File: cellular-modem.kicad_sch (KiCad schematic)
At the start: 44 parts, among them J1 Conn_Coaxial, J2 SIM8060-6-1-14-00-A, Q1 BC818, SW1 KMR221GLFS, U2 EG25G

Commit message: Add: Improved layout
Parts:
- removed J1: Conn_Coaxial, Connector_Coaxial:U.FL_Hirose_U.FL-R-SMT-1_Vertical, symbol Connector:Conn_Coaxial
- removed TP3: DCD, TestPoint:TestPoint_Pad_D1.5mm, symbol Connector:TestPoint
- removed TP4: CTS, TestPoint:TestPoint_Pad_D1.5mm, symbol Connector:TestPoint
- removed TP5: RTS, TestPoint:TestPoint_Pad_D1.5mm, symbol Connector:TestPoint
- removed TP6: DTR, TestPoint:TestPoint_Pad_D1.5mm, symbol Connector:TestPoint
- added E1: NN02-201, NN02-201:XCVR_NN02-201, symbol NN02-201:NN02-201
- TP1, TP10, TP7, TP8, TP9: footprint TestPoint:TestPoint_Pad_D1.5mm -> TestPoint:TestPoint_Pad_1.0x1.0mm
- TP2: value RI -> 3V8; footprint TestPoint:TestPoint_Pad_D1.5mm -> TestPoint:TestPoint_Pad_1.0x1.0mm
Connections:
- net +3V8: now also TP2.1
- net at C14.1, L2.1: now also E1.1
- net at U2.62 (RI): no longer TP2.1
- no-connect marks 54 -> 59

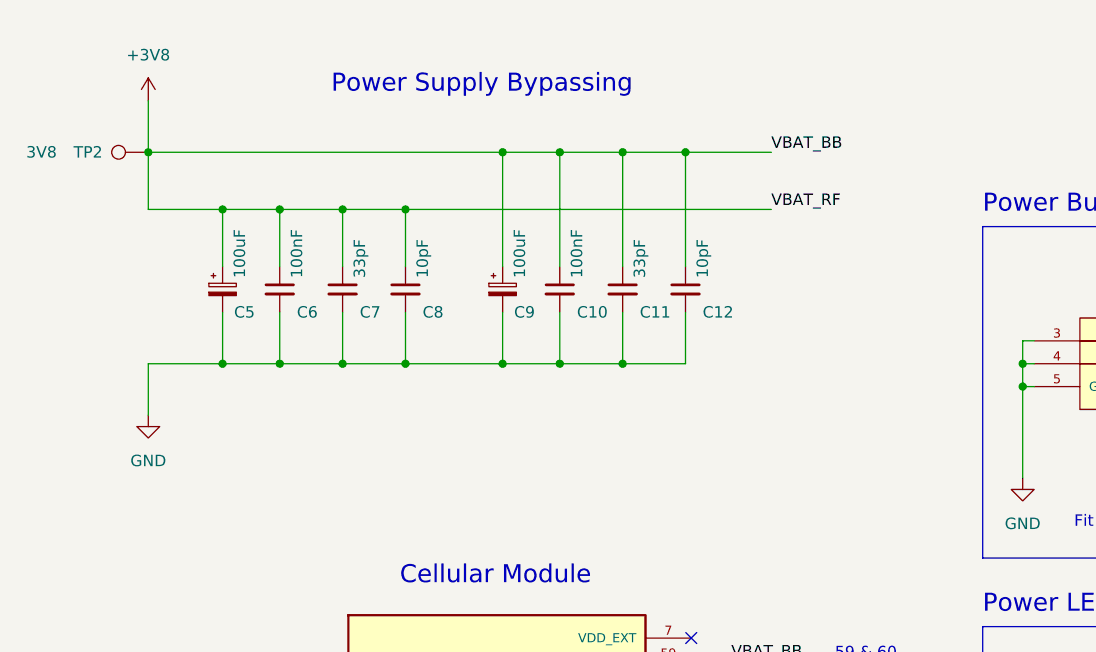
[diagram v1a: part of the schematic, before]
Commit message: Update: Ground plane setup
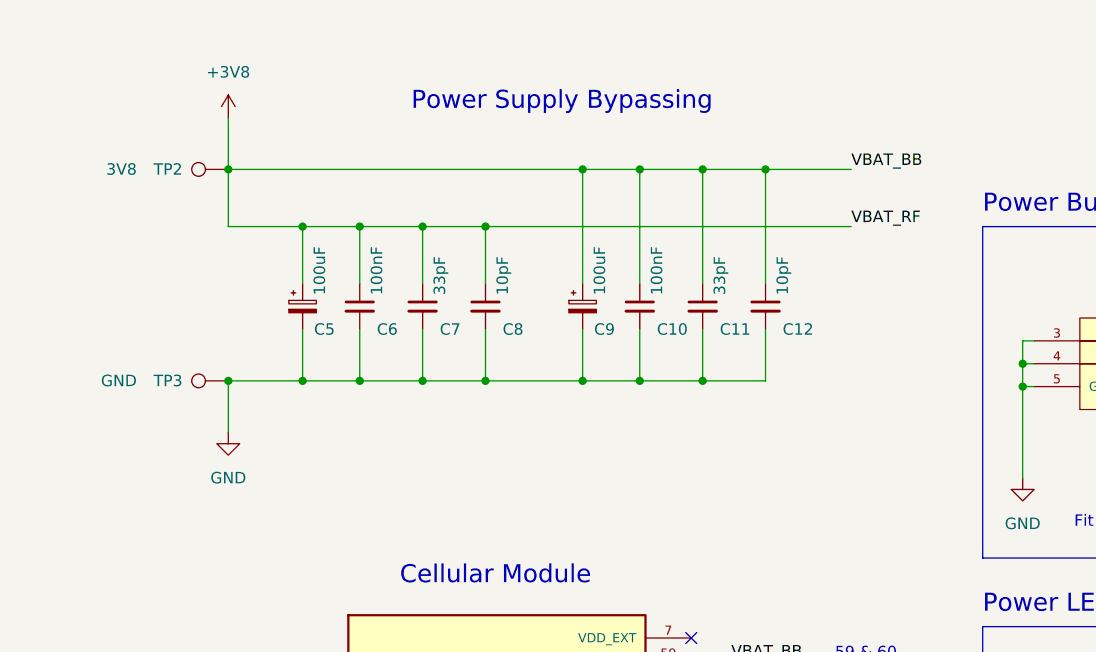
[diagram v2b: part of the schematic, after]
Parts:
- added TP3: GND, TestPoint:TestPoint_Pad_1.0x1.0mm, symbol Connector:TestPoint
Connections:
- net GND: now also TP3.1
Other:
- moved on the sheet: C10, C11, C12, C5, C6, C7, C8, C9, TP2

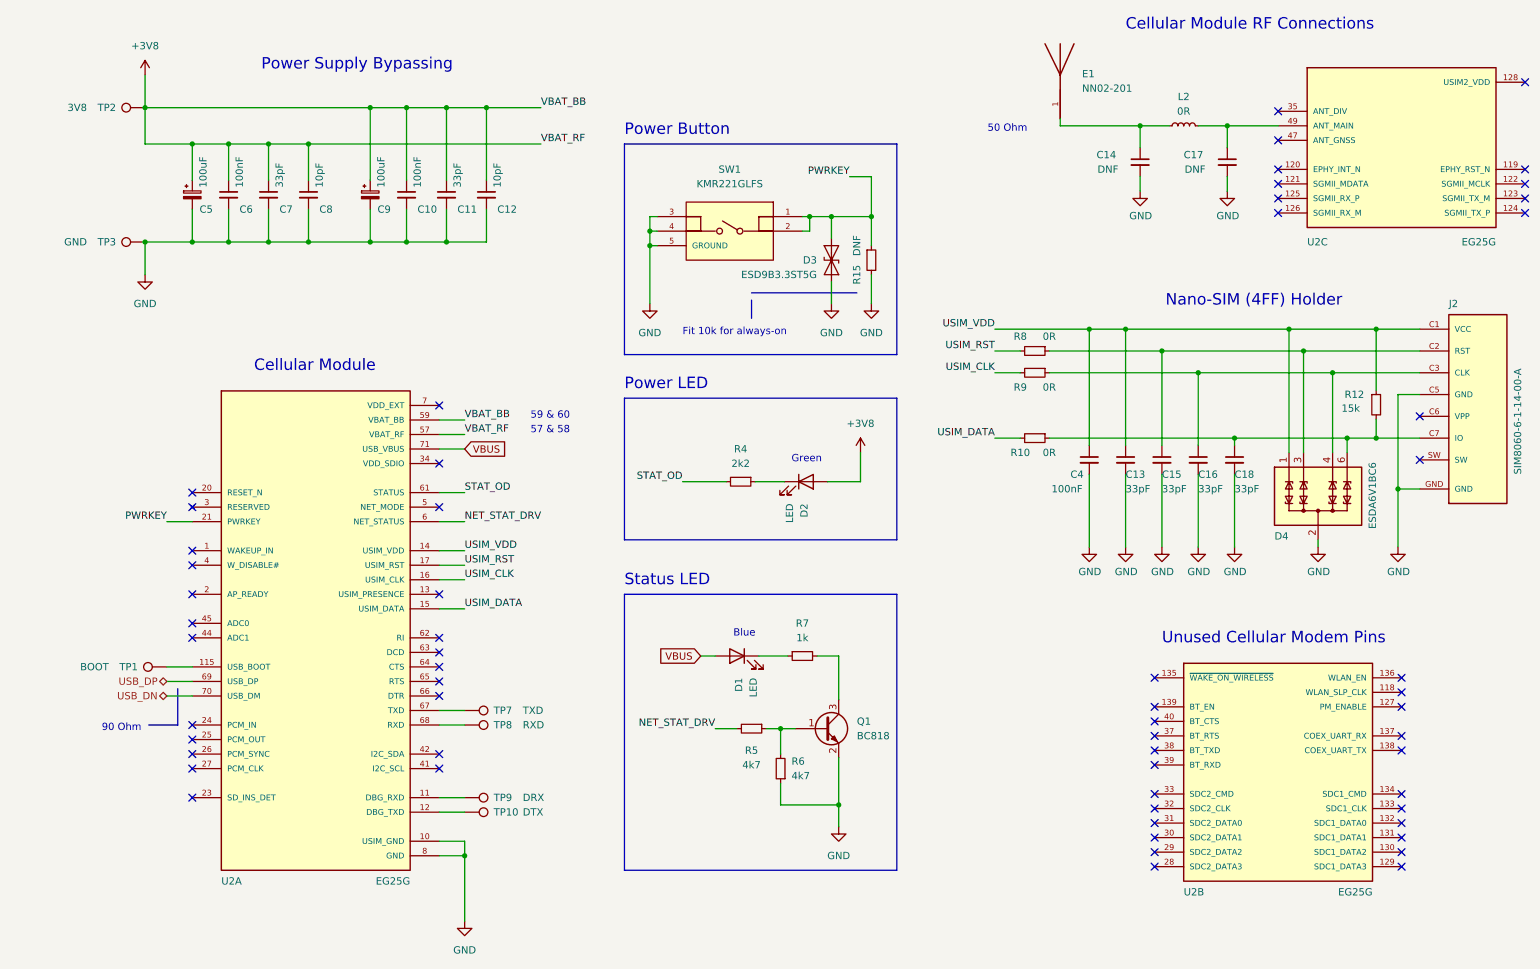
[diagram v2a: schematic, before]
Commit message: Add: Board size changes
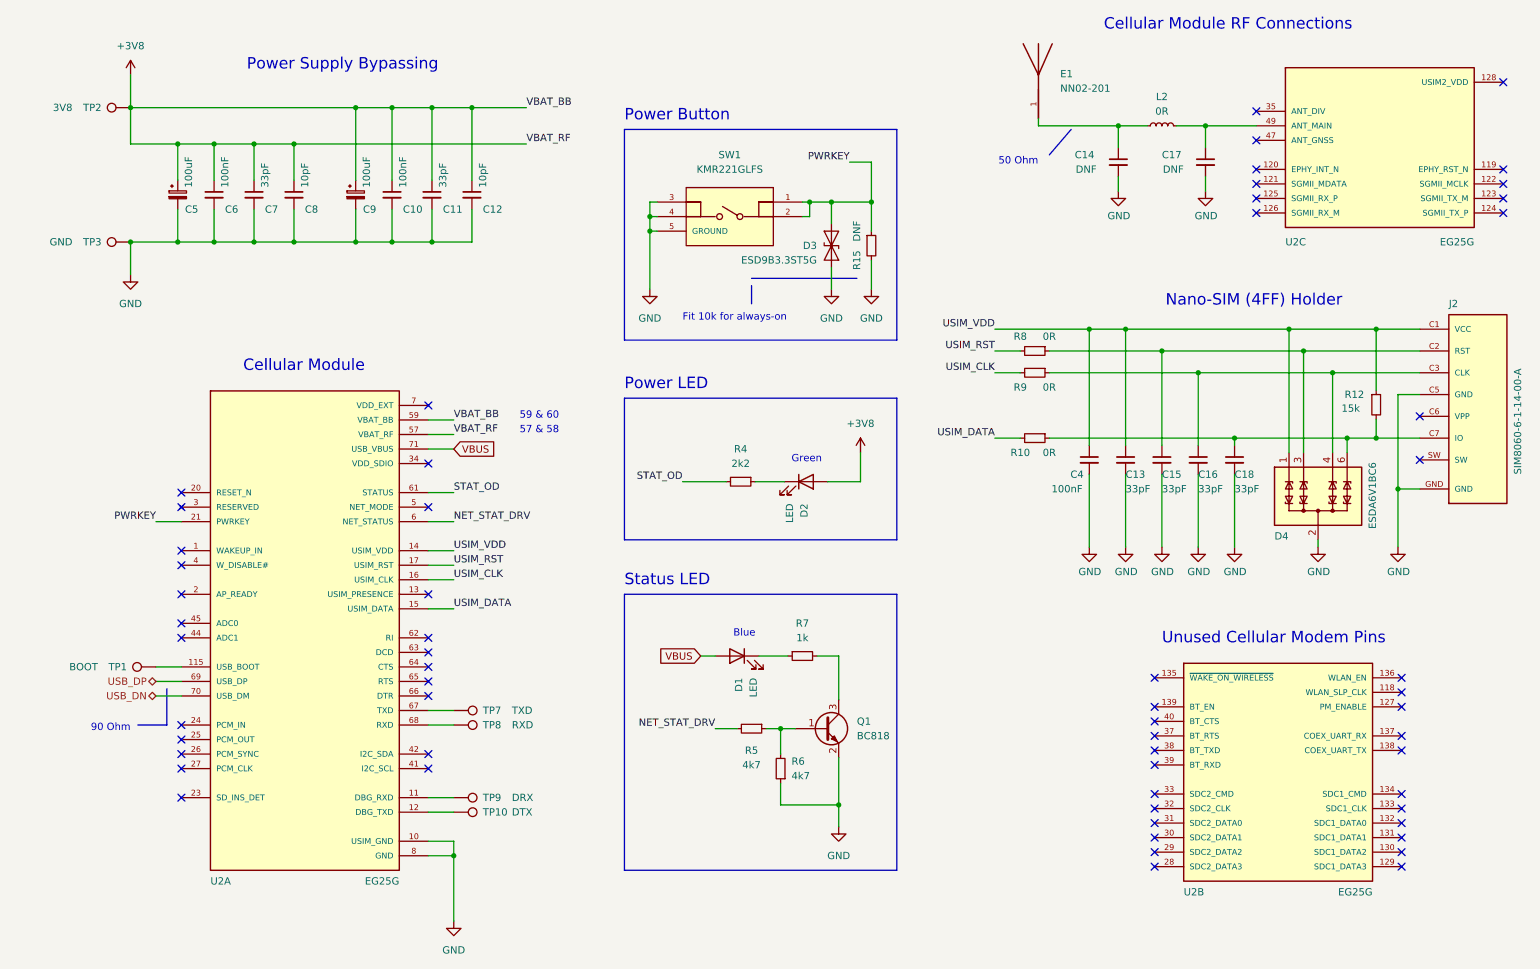
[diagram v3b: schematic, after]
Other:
- moved on the sheet: C10, C11, C12, C14, C17, C5, C6, C7, C8, C9, D3, E1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

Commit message: Change: Separate boards rather than using mousebites
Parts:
- C10, C4, C6: Int @ 10 (none) -> 0.038; MPN (none) -> C0603C104K3RAC; Mfr (none) -> KEMET; SKU (none) -> 80-C0603C104K3RAC; Stock Situation (none) -> OK @ 2Nov2022; Vendor (none) -> Mouser
- C11, C7: Int @ 10 (none) -> 0.026; MPN (none) -> 06035A330KAT2A; Mfr (none) -> AVX; SKU (none) -> 581-06035A330K; Stock Situation (none) -> OK @ 2Nov2022; Vendor (none) -> Mouser
- C13, C15, C16, C18: Int @ 10 0.023 -> 0.026; SKU 581-06035A330KAT2A -> 581-06035A330K; Stock Situation (none) -> OK @ 2Nov2022
- C5, C9: Int @ 10 (none) -> 0.62; MPN (none) -> TCJB107M006R0040; Mfr (none) -> Kyocera/AVX; SKU (none) -> 581-TCJB107M006R0040; Stock Situation (none) -> OK @ 2Nov2022; Vendor (none) -> Mouser
- D3: Int @ 10 (none) -> 0.187; MPN (none) -> ESD9B3.3ST5G; Mfr (none) -> ON Semiconductor; SKU (none) -> 863-ESD9B3.3ST5G; Stock Situation (none) -> OK @ 2Nov2022; Vendor (none) -> Mouser
- D4: Int @ 10 (none) -> 0.353; MPN (none) -> ESDA6V1BC6; Mfr (none) -> STMicroelectronics; SKU (none) -> 511-ESDA6V1BC6; Stock Situation (none) -> OK @ 2Nov2022; Vendor (none) -> Mouser
- E1: Int @ 10 (none) -> 1.01; MANUFACTURER FRACTUS ANTENNAS -> (none); MAXIMUM_PACKAGE_HEIGHT 1.0mm -> (none); MPN (none) -> NN02-201; Mfr (none) -> Ignion Inc.; PARTREV December 2020 -> (none); SKU (none) -> 128-NN02-201; STANDARD Manufacturer recommendations -> (none); Stock Situation (none) -> OK @ 2Nov2022; Vendor (none) -> Mouser
- J2: Int @ 10 (none) -> 1.02; MANUFACTURER GCT -> (none); MPN (none) -> SIM8060-6-1-14-00-A; Mfr (none) -> GCT; PARTREV A -> (none); SKU (none) -> 640-SIM8060611400A; STANDARD Manufacturer recommendations -> (none); Stock Situation (none) -> OK @ 2Nov2022; Vendor (none) -> Mouser
- Q1: Int @ 10 (none) -> 0.436; MPN (none) -> BC818-40; Mfr (none) -> Diotec Semiconductor Inc; SKU (none) -> 637-BC818-40; Stock Situation (none) -> OK @ 2Nov2022; Vendor (none) -> Mouser
- SW1: Int @ 10 (none) -> 0.352; MPN (none) -> KMR221GLFS; Mfr (none) -> C&K; SKU (none) -> 611-KMR221G-LFS; Stock Situation (none) -> OK @ 2Nov2022; Vendor (none) -> Mouser
- U2: Int @ 10 (none) -> 20.00; MPN (none) -> EG25G; Mfr (none) -> Quectel Wireless Solutions Inc.; Vendor (none) -> AliExpress
